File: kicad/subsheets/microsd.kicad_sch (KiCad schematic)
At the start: 17 parts

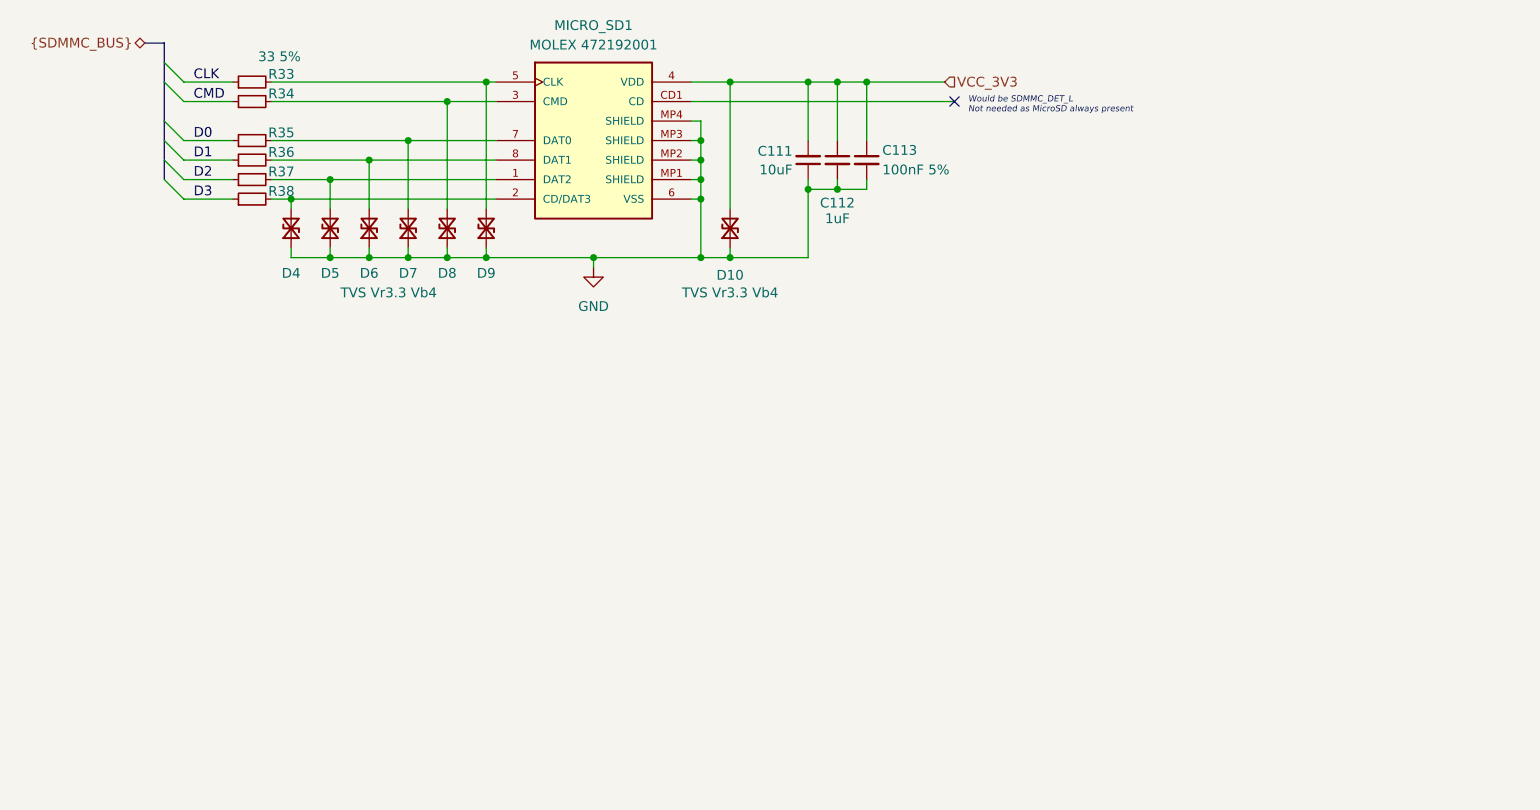
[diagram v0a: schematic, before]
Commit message: Change all sheets to A4, name sheets, split RK3566 into hierarchy
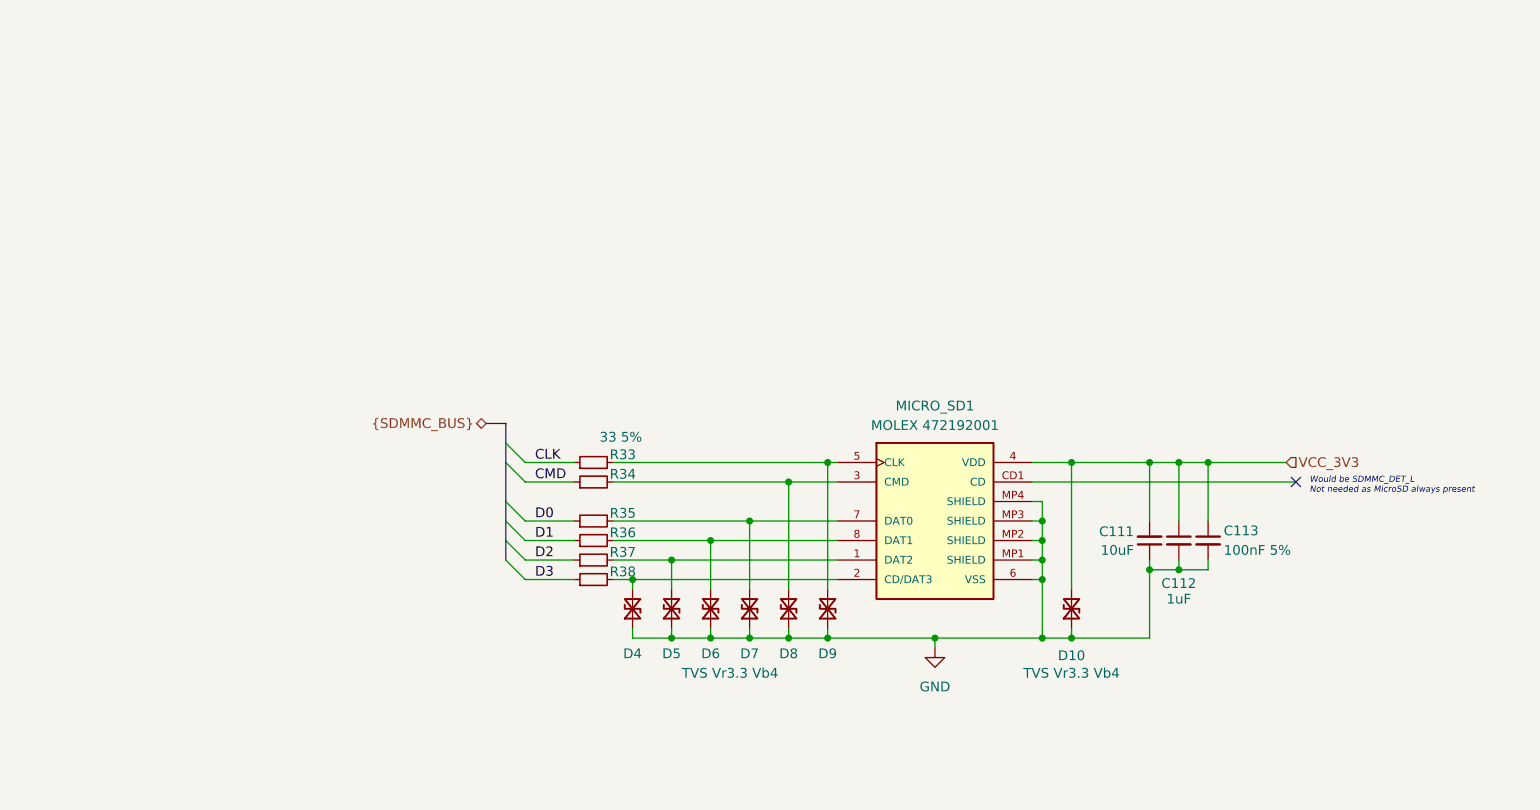
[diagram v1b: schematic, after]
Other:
- title: (none) -> MicroSD Card Enclosure
- moved on the sheet: C111, C112, C113, D10, D4, D5, D6, D7, D8, D9, MICRO_SD1, R33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

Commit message: Mark as R1.0
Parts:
- renumbered C111 to C153, C112 to C154, C113 to C155, R33 to R47, R34 to R48, R35 to R49, R36 to R50, R37 to R51, R38 to R52
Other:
- company: (none) -> UVic Rocketry
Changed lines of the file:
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@@
 	(title_block
 		(title "MicroSD Card Enclosure")
+		(date "2025-11-23")
+		(rev "1.0")
+		(company "UVic Rocketry")
+		(comment 1 "Author: Eric Handley")
 	)
 	(text "Would be SDMMC_DET_L\nNot needed as MicroSD always present"
@@
 		(on_board yes)
 		(dnp no)
-		(property "Reference" "R34"
+		(property "Reference" "R48"
 			(at 110.49 86.614 90)
 			(effects
@@
 			(project "srad-camera"
 				(path "/da62c771-e8c9-451f-8df1-ec995aadcb11/f62984d3-000f-4116-a13f-09b83b0ce025"
-					(reference "R34")
+					(reference "R48")
 					(unit 1)
 				)
@@
 		(on_board yes)
 		(dnp no)
-		(property "Reference" "R33"
+		(property "Reference" "R47"
 			(at 110.49 84.074 90)
 			(effects
@@
 			(project "srad-camera"
 				(path "/da62c771-e8c9-451f-8df1-ec995aadcb11/f62984d3-000f-4116-a13f-09b83b0ce025"
-					(reference "R33")
+					(reference "R47")
 					(unit 1)
 				)
@@
 		(on_board yes)
 		(dnp no)
-		(property "Reference" "C113"
+		(property "Reference" "C155"
 			(at 188.722 93.98 0)
 			(effects
@@
 			(project "srad-camera"
 				(path "/da62c771-e8c9-451f-8df1-ec995aadcb11/f62984d3-000f-4116-a13f-09b83b0ce025"
-					(reference "C113")
+					(reference "C155")
 					(unit 1)
 				)
@@
 		(on_board yes)
 		(dnp no)
-		(property "Reference" "R36"
+		(property "Reference" "R50"
 			(at 110.49 94.234 90)
 			(effects
@@
 			(project "srad-camera"
 				(path "/da62c771-e8c9-451f-8df1-ec995aadcb11/f62984d3-000f-4116-a13f-09b83b0ce025"
-					(reference "R36")
+					(reference "R50")
 					(unit 1)
 				)
@@
 		(dnp no)
 		(fields_autoplaced yes)
-		(property "Reference" "#PWR059"
+		(property "Reference" "#PWR095"
 			(at 151.13 115.57 0)
 			(effects
@@
 			(project "srad-camera"
 				(path "/da62c771-e8c9-451f-8df1-ec995aadcb11/f62984d3-000f-4116-a13f-09b83b0ce025"
-					(reference "#PWR059")
+					(reference "#PWR095")
 					(unit 1)
 				)
@@
 		(on_board yes)
 		(dnp no)
-		(property "Reference" "R35"
+		(property "Reference" "R49"
 			(at 110.49 91.694 90)
 			(effects
@@
 			(project "srad-camera"
 				(path "/da62c771-e8c9-451f-8df1-ec995aadcb11/f62984d3-000f-4116-a13f-09b83b0ce025"
-					(reference "R35")
+					(reference "R49")
 					(unit 1)
 				)
@@
 		(on_board yes)
 		(dnp no)
-		(property "Reference" "C112"
+		(property "Reference" "C154"
 			(at 182.88 100.838 0)
 			(effects
@@
 			(project "srad-camera"
 				(path "/da62c771-e8c9-451f-8df1-ec995aadcb11/f62984d3-000f-4116-a13f-09b83b0ce025"
-					(reference "C112")
+					(reference "C154")
 					(unit 1)
 				)
@@
 		(on_board yes)
 		(dnp no)
-		(property "Reference" "R37"
+		(property "Reference" "R51"
 			(at 110.49 96.774 90)
 			(effects
@@
 			(project "srad-camera"
 				(path "/da62c771-e8c9-451f-8df1-ec995aadcb11/f62984d3-000f-4116-a13f-09b83b0ce025"
-					(reference "R37")
+					(reference "R51")
 					(unit 1)
 				)
@@
 		(on_board yes)
 		(dnp no)
-		(property "Reference" "C111"
+		(property "Reference" "C153"
 			(at 177.038 94.0957 0)
 			(effects
@@
 			(project "srad-camera"
 				(path "/da62c771-e8c9-451f-8df1-ec995aadcb11/f62984d3-000f-4116-a13f-09b83b0ce025"
-					(reference "C111")
+					(reference "C153")
 					(unit 1)
 				)
@@
 		(on_board yes)
 		(dnp no)
-		(property "Reference" "R38"
+		(property "Reference" "R52"
 			(at 110.49 99.314 90)
 			(effects
@@
 			(project "srad-camera"
 				(path "/da62c771-e8c9-451f-8df1-ec995aadcb11/f62984d3-000f-4116-a13f-09b83b0ce025"
-					(reference "R38")
+					(reference "R52")
 					(unit 1)
 				)

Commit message: Annotations
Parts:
- renumbered C153 to C167, C154 to C168, C155 to C169, R47 to R54, R48 to R55, R49 to R56, R50 to R57, R51 to R58, R52 to R59
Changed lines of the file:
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@@
 		(on_board yes)
 		(dnp no)
-		(property "Reference" "R48"
+		(property "Reference" "R55"
 			(at 110.49 86.614 90)
 			(effects
@@
 			(project "srad-camera"
 				(path "/da62c771-e8c9-451f-8df1-ec995aadcb11/f62984d3-000f-4116-a13f-09b83b0ce025"
-					(reference "R48")
+					(reference "R55")
 					(unit 1)
 				)
@@
 		(on_board yes)
 		(dnp no)
-		(property "Reference" "R47"
+		(property "Reference" "R54"
 			(at 110.49 84.074 90)
 			(effects
@@
 			(project "srad-camera"
 				(path "/da62c771-e8c9-451f-8df1-ec995aadcb11/f62984d3-000f-4116-a13f-09b83b0ce025"
-					(reference "R47")
+					(reference "R54")
 					(unit 1)
 				)
@@
 		(on_board yes)
 		(dnp no)
-		(property "Reference" "C155"
+		(property "Reference" "C169"
 			(at 188.722 93.98 0)
 			(effects
@@
 			(project "srad-camera"
 				(path "/da62c771-e8c9-451f-8df1-ec995aadcb11/f62984d3-000f-4116-a13f-09b83b0ce025"
-					(reference "C155")
+					(reference "C169")
 					(unit 1)
 				)
@@
 		(on_board yes)
 		(dnp no)
-		(property "Reference" "R50"
+		(property "Reference" "R57"
 			(at 110.49 94.234 90)
 			(effects
@@
 			(project "srad-camera"
 				(path "/da62c771-e8c9-451f-8df1-ec995aadcb11/f62984d3-000f-4116-a13f-09b83b0ce025"
-					(reference "R50")
+					(reference "R57")
 					(unit 1)
 				)
@@
 		(dnp no)
 		(fields_autoplaced yes)
-		(property "Reference" "#PWR095"
+		(property "Reference" "#PWR0107"
 			(at 151.13 115.57 0)
 			(effects
@@
 			(project "srad-camera"
 				(path "/da62c771-e8c9-451f-8df1-ec995aadcb11/f62984d3-000f-4116-a13f-09b83b0ce025"
-					(reference "#PWR095")
+					(reference "#PWR0107")
 					(unit 1)
 				)
@@
 		(on_board yes)
 		(dnp no)
-		(property "Reference" "R49"
+		(property "Reference" "R56"
 			(at 110.49 91.694 90)
 			(effects
@@
 			(project "srad-camera"
 				(path "/da62c771-e8c9-451f-8df1-ec995aadcb11/f62984d3-000f-4116-a13f-09b83b0ce025"
-					(reference "R49")
+					(reference "R56")
 					(unit 1)
 				)
@@
 		(on_board yes)
 		(dnp no)
-		(property "Reference" "C154"
+		(property "Reference" "C168"
 			(at 182.88 100.838 0)
 			(effects
@@
 			(project "srad-camera"
 				(path "/da62c771-e8c9-451f-8df1-ec995aadcb11/f62984d3-000f-4116-a13f-09b83b0ce025"
-					(reference "C154")
+					(reference "C168")
 					(unit 1)
 				)
@@
 		(on_board yes)
 		(dnp no)
-		(property "Reference" "R51"
+		(property "Reference" "R58"
 			(at 110.49 96.774 90)
 			(effects
@@
 			(project "srad-camera"
 				(path "/da62c771-e8c9-451f-8df1-ec995aadcb11/f62984d3-000f-4116-a13f-09b83b0ce025"
-					(reference "R51")
+					(reference "R58")
 					(unit 1)
 				)
@@
 		(on_board yes)
 		(dnp no)
-		(property "Reference" "C153"
+		(property "Reference" "C167"
 			(at 177.038 94.0957 0)
 			(effects
@@
 			(project "srad-camera"
 				(path "/da62c771-e8c9-451f-8df1-ec995aadcb11/f62984d3-000f-4116-a13f-09b83b0ce025"
-					(reference "C153")
+					(reference "C167")
 					(unit 1)
 				)
@@
 		(on_board yes)
 		(dnp no)
-		(property "Reference" "R52"
+		(property "Reference" "R59"
 			(at 110.49 99.314 90)
 			(effects
@@
 			(project "srad-camera"
 				(path "/da62c771-e8c9-451f-8df1-ec995aadcb11/f62984d3-000f-4116-a13f-09b83b0ce025"
-					(reference "R52")
+					(reference "R59")
 					(unit 1)
 				)

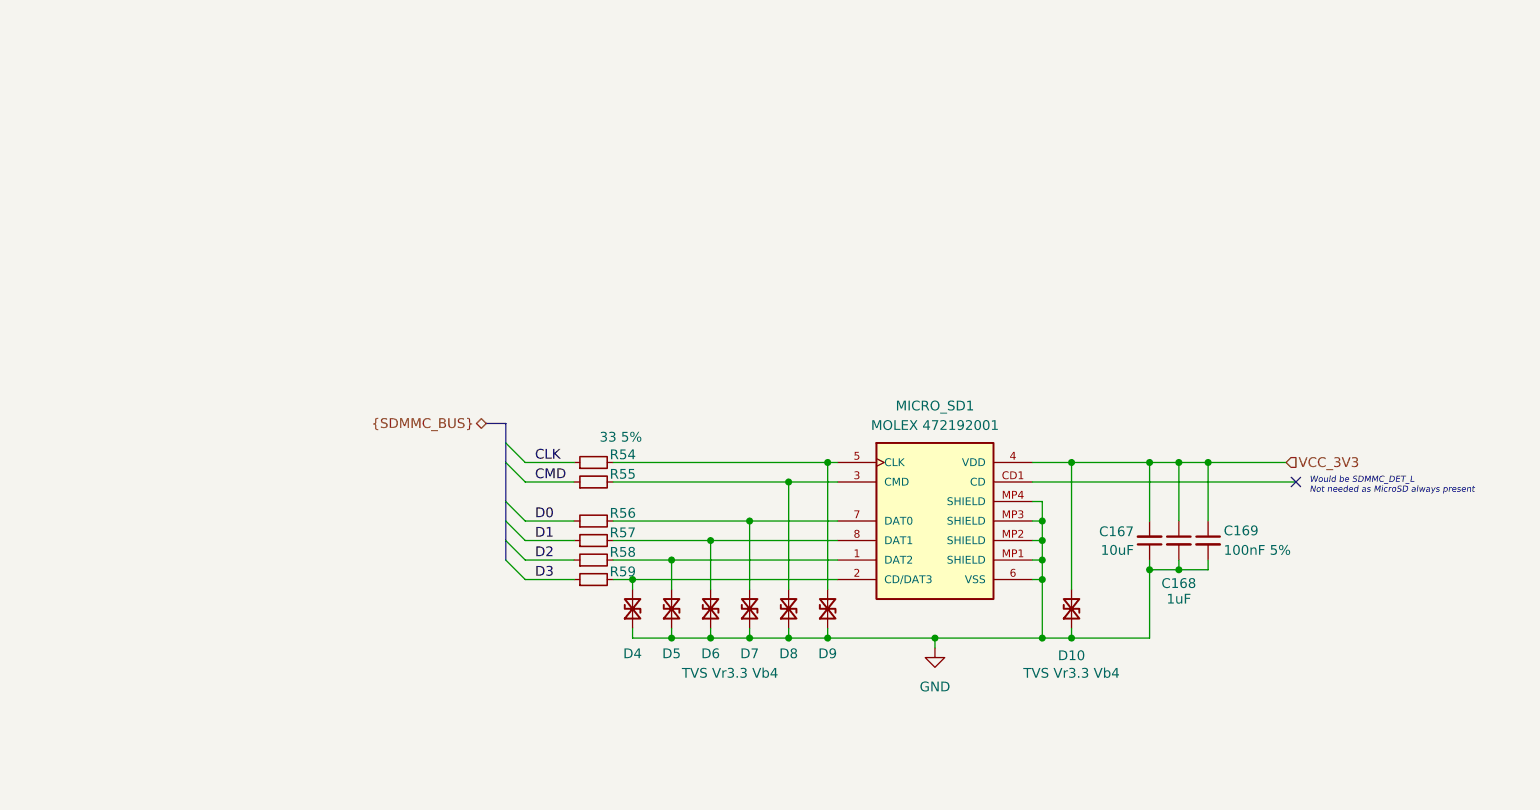
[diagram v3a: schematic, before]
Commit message: Swap for standard library symbol
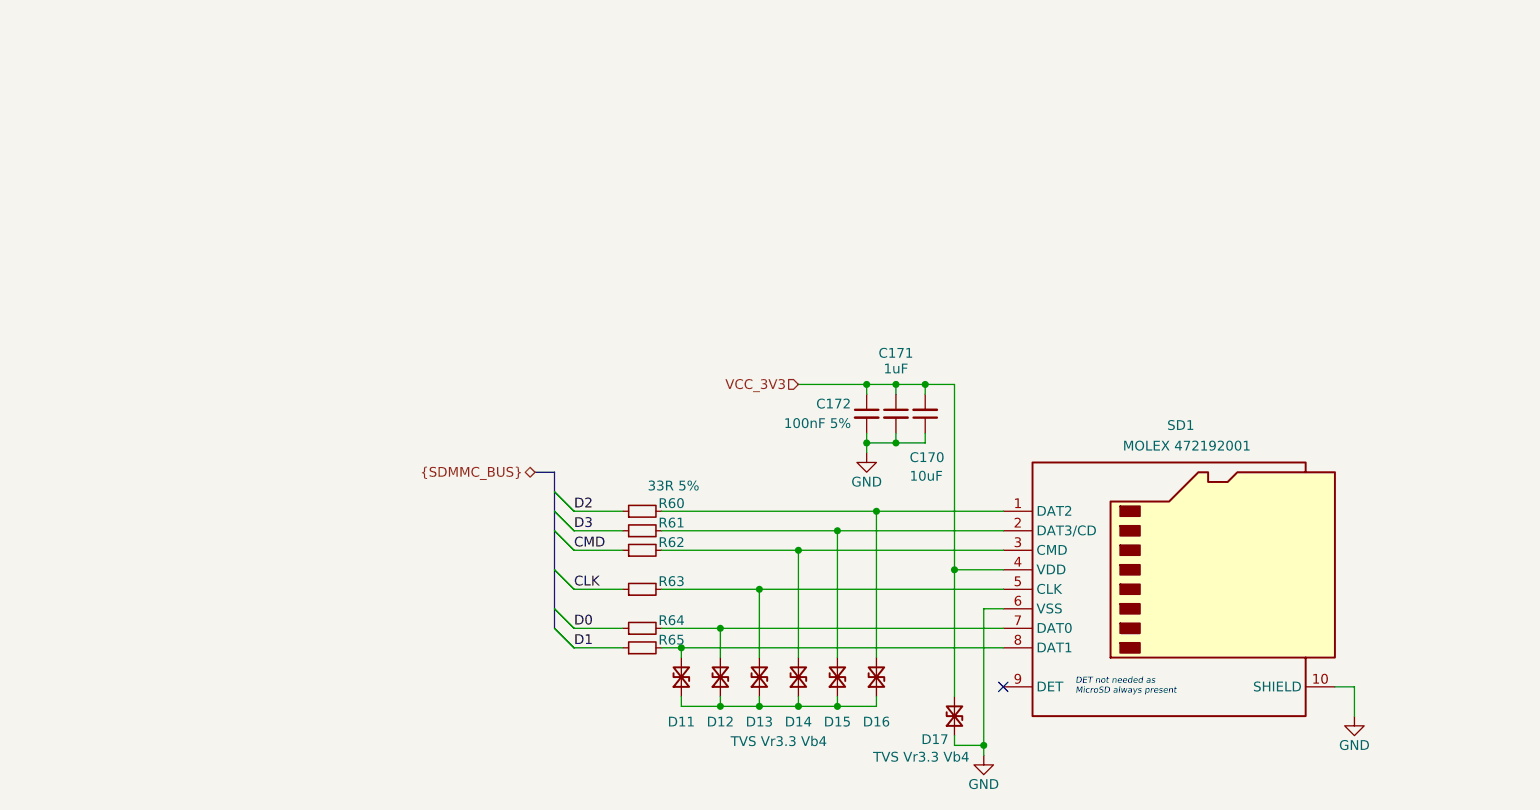
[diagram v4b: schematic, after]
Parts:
- removed C167: 10uF, Capacitor_SMD:C_0603_1608Metric, symbol Device:C_Small
- removed C168: 1uF, Capacitor_SMD:C_0402_1005Metric, symbol Device:C_Small
- removed C169: 100nF 5%, Capacitor_SMD:C_0201_0603Metric, symbol Device:C_Small
- removed D10, D4, D5, D6, D7, D8, D9: TVS Vr3.3 Vb4, Resistor_SMD:R_0201_0603Metric, symbol Device:D_TVS_Small
- removed MICRO_SD1: MOLEX 472192001, Connector_Card:microSD_HC_Molex_47219-2001, symbol TF-01A:TF-01A
- removed R54, R55, R56, R57, R58, R59: 33 5%, Resistor_SMD:R_0402_1005Metric, symbol Device:R_Small
- added C170: 10uF, Capacitor_SMD:C_0603_1608Metric, symbol Device:C_Small
- added C171: 1uF, Capacitor_SMD:C_0402_1005Metric, symbol Device:C_Small
- added C172: 100nF 5%, Capacitor_SMD:C_0201_0603Metric, symbol Device:C_Small
- added D11, D12, D13, D14, D15, D16, D17: TVS Vr3.3 Vb4, Resistor_SMD:R_0201_0603Metric, symbol Device:D_TVS_Small
- added R60, R61, R62, R63, R64: 33 5%, Resistor_SMD:R_0402_1005Metric, symbol Device:R_Small
- added R65: 33R 5%, Resistor_SMD:R_0402_1005Metric, symbol Device:R_Small
- added SD1: MOLEX 472192001, Connector_Card:microSD_HC_Molex_47219-2001, symbol Connector:Micro_SD_Card_Det1
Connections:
- net CLK: now also R63.1
- net CMD: now also R62.1
- net D0: now also R64.1
- net D1: now also R65.1
- net D2: now also R60.1
- net D3: now also R61.1
- net GND: now also C170.1, C171.2, C172.2, D17.1 (A1), SD1.10 (SHIELD), SD1.6 (VSS)
- net VCC_3V3: now also C170.2, C171.1, C172.1, D17.2 (A2), SD1.4 (VDD)
- new net: D11.1 (A1), D12.1 (A1), D13.1 (A1), D14.1 (A1), D15.1 (A1), D16.1 (A1)
- new net: D14.2 (A2), R62.2, SD1.3 (CMD)
- new net: D15.2 (A2), R61.2, SD1.2 (DAT3/CD)
- new net: D11.2 (A2), R65.2, SD1.8 (DAT1)
- new net: D12.2 (A2), R64.2, SD1.7 (DAT0)
- new net: D13.2 (A2), R63.2, SD1.5 (CLK)
- new net: D16.2 (A2), R60.2, SD1.1 (DAT2)
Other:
- note added: "DET not needed as MicroSD always present"
- note removed: "Would be SDMMC_DET_L Not needed as MicroSD always present"

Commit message: Start on PCB design
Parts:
- C165: renamed from C172; value 100nF 5% -> 100nF; footprint Capacitor_SMD:C_0201_0603Metric -> Capacitor_SMD:C_0402_1005Metric; LCSC PART NAME (none) -> C1525
- C166: renamed from C171; footprint Capacitor_SMD:C_0402_1005Metric -> Capacitor_SMD:C_0603_1608Metric; LCSC PART NAME (none) -> C15849
- C167: renamed from C170; footprint Capacitor_SMD:C_0603_1608Metric -> Capacitor_SMD:C_0805_2012Metric; LCSC PART NAME (none) -> C15850
- D10: renamed from D17; footprint Resistor_SMD:R_0201_0603Metric -> Diode_SMD:D_SOD-123F; LCSC PART NAME (none) -> C19077496
- D4: renamed from D11; footprint Resistor_SMD:R_0201_0603Metric -> Diode_SMD:D_SOD-123F; LCSC PART NAME (none) -> C19077496
- D5: renamed from D12; footprint Resistor_SMD:R_0201_0603Metric -> Diode_SMD:D_SOD-123F; LCSC PART NAME (none) -> C19077496
- D6: renamed from D13; footprint Resistor_SMD:R_0201_0603Metric -> Diode_SMD:D_SOD-123F; LCSC PART NAME (none) -> C19077496
- D7: renamed from D14; footprint Resistor_SMD:R_0201_0603Metric -> Diode_SMD:D_SOD-123F; LCSC PART NAME (none) -> C19077496
- D8: renamed from D15; footprint Resistor_SMD:R_0201_0603Metric -> Diode_SMD:D_SOD-123F; LCSC PART NAME (none) -> C19077496
- D9: renamed from D16; footprint Resistor_SMD:R_0201_0603Metric -> Diode_SMD:D_SOD-123F; LCSC PART NAME (none) -> C19077496
- R56: renamed from R60; value 33 5% -> 22R; LCSC PART NAME (none) -> C25092
- R57: renamed from R61; value 33 5% -> 22R; LCSC PART NAME (none) -> C25092
- R58: renamed from R62; value 33 5% -> 22R; LCSC PART NAME (none) -> C25092
- R59: renamed from R63; value 33 5% -> 22R; LCSC PART NAME (none) -> C25092
- R60: renamed from R64; value 33 5% -> 22R; LCSC PART NAME (none) -> C25092
- R61: renamed from R65; value 33R 5% -> 22R; LCSC PART NAME (none) -> C25092
